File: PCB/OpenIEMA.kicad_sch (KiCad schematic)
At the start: 63 parts, among them J1 Battery, J2 XLR3, J3 USB_C_Receptacle_PowerOnly_6P, J4 AudioJack3, J5 AudioJack3, SW2 SW_SPDT, U1 MCP73831-2-MC, U2 TPS61023DRLR, U3 OPA1678, U4 TPA6132A2RTE

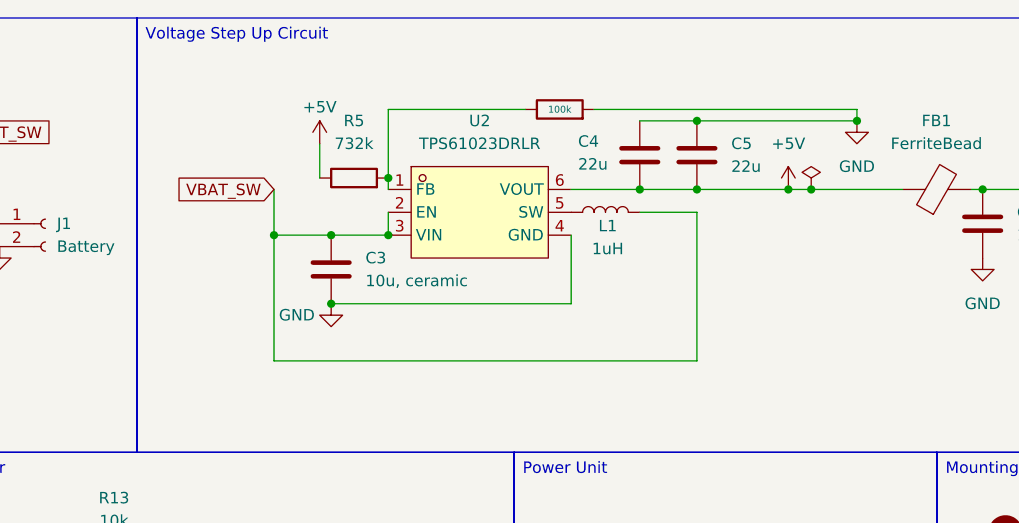
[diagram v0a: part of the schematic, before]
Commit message: New PCB layout and routing + schematic cleanup
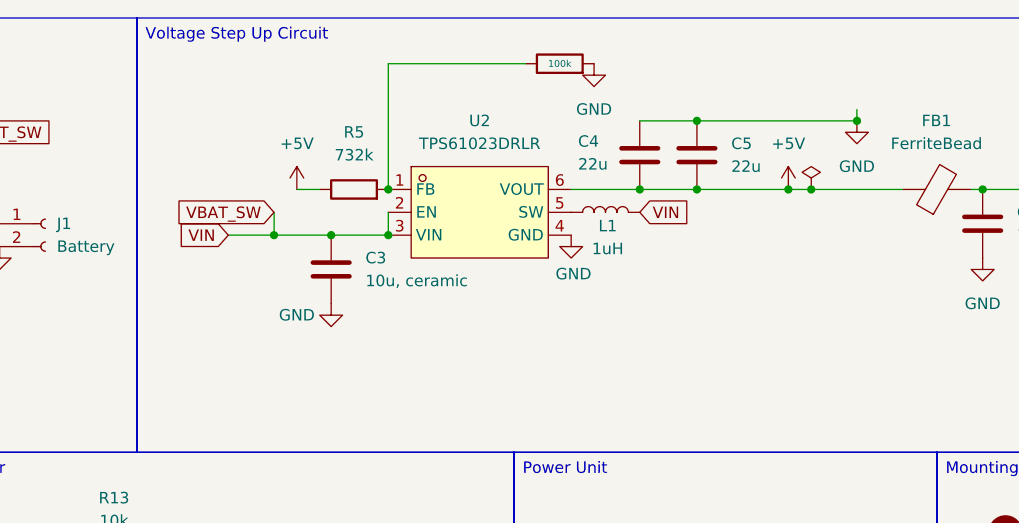
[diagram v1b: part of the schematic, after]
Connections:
- net GND: now also C17.1; no longer C17.2
- net at U4.8 (HPVSS): now also C17.2; no longer C17.1
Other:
- moved on the sheet: C17, R5
